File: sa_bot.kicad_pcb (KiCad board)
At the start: 2 copper layers, 120 x 120 mm, 68 parts, among them CON1 MicroSD_Card, P1 USB_OTG, P11 MOTOR_A, P12 MOTOR_B, P13 SONAR_4, P14 SONAR_2, P15 SONAR_3, P17 DBG_CONN, P18 CONN_01X04, P2 BatteryHolder, P3 IR4_JMP, P4 IR2_JMP, P5 IR3_JMP, P6 ExPower, P7 IR_4, P8 IR_2, P9 IR_3, Q1 Q_PMOS_DSG, SW1 SWITCH_INV, SW2 SW_PUSH, SW3 SW_PUSH, SW4 SW_PUSH, U1 74AHC1G125, U2 SAMD21G18, U3 AP2112K-3.3V, U4 NCP1402, U5 DRV8835, Y1 Crystal_Small

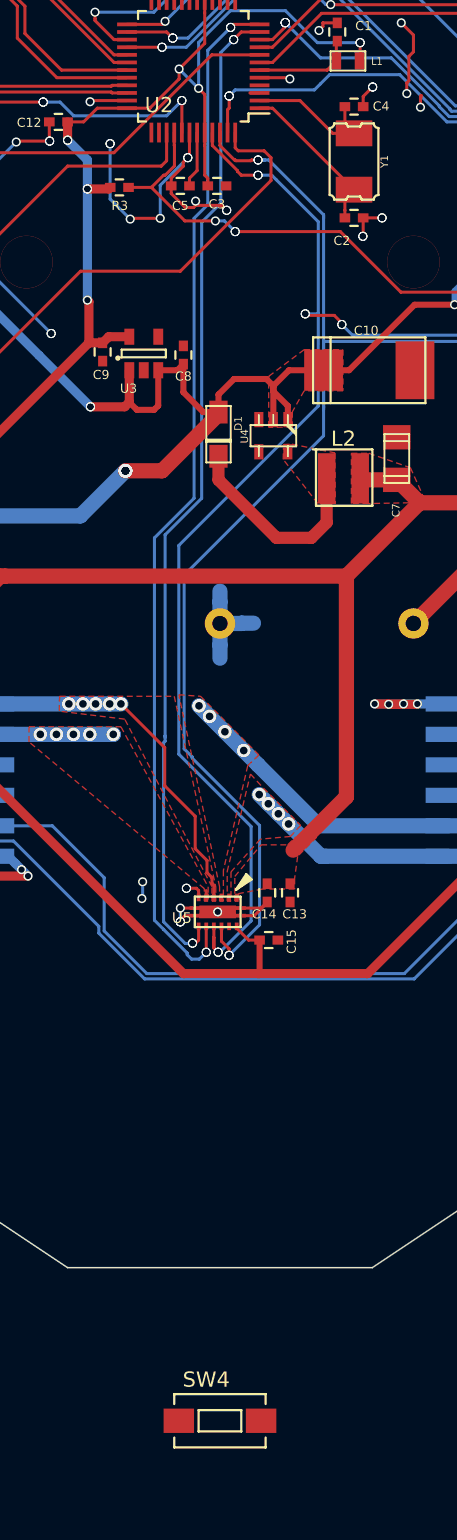
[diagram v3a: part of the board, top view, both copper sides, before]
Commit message: Moved Motor from SWCLK to A0
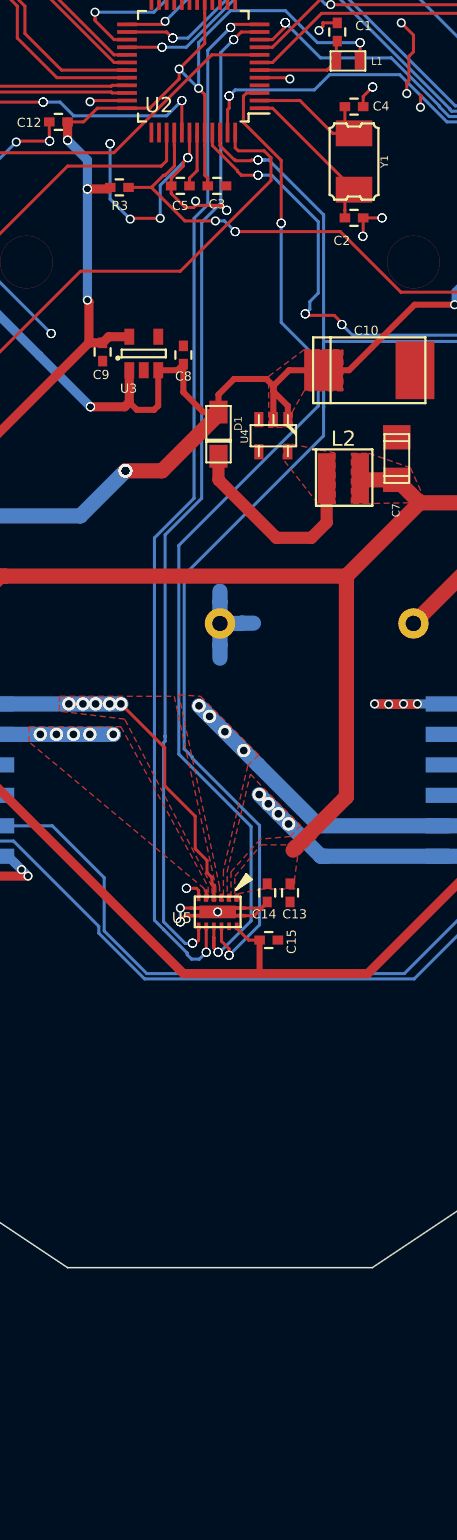
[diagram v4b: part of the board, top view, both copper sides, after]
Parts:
- removed the SW4 at (140.0, 230.1)
- renumbered RESET to SW4
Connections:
- U2 pad 3: Net-(U2-Pad3) -> /AIN2
- U5 pad 9: SWCLK -> /AIN2
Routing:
- net /AIN2: track 0.00 -> 69.1 mm, vias 0 -> 4
- net SWCLK: track 86.1 -> 34.6 mm, vias 8 -> 6
- net (no net): track 7.58 -> 6.42 mm, vias 5 -> 3
- net Net-(U2-Pad3): track 0.64 -> 0.00 mm

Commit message: V002 and firmware
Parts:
- P17: footprint Pin_Headers:Pin_Header_Straight_2x05_Pitch1.27mm -> idlehands_footprints:Pin_Header_Straight_2x05_Pitch1.27mm
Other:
- board text added: "Neural Adaptation Bot v0.02 McMaster University Idle Hands Dev. 11/01/2016"
- board text removed: "Neural Adaptation Bot McMaster University Idle Hands Dev. 04/06/2016"
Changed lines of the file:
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@@
-(kicad_pcb (version 4) (host pcbnew "(2015-07-04 BZR 5884, Git c1bbf3e)-product")
+(kicad_pcb (version 4) (host pcbnew 4.0.4-stable)
   (general
     (links 168)
-    (no_connects 8)
-    (area 79.949999 99.949999 200.050001 220.050001)
+    (no_connects 7)
+    (area 63.774999 83.774999 219.485112 246.000001)
     (thickness 1.6)
     (drawings 17)
@@
     )
   )
-  (module Pin_Headers:Pin_Header_Straight_2x05_Pitch1.27mm (layer F.Cu)
-    (at 164.07 159.2 180)
-    (descr "Through hole pin header, pitch 1.27mm")
-    (tags "pin header")
-    (fp_text reference P17 (at 0.55 -1.7 180) (layer F.SilkS)
-      (effects (font (size 1 1) (thickness 0.15)))
-    )
-    (fp_text value DBG_CONN (at 0 6.9 180) (layer F.Fab)
-      (effects (font (size 1 1) (thickness 0.15)))
-    )
-    (fp_line (start 2.1 -0.8) (end 1.3 -0.8) (layer F.SilkS) (width 0.15))
-    (fp_line (start 2.1 5.85) (end 2.1 -0.8) (layer F.SilkS) (width 0.15))
-    (fp_line (start 2.1 5.85) (end -0.85 5.85) (layer F.SilkS) (width 0.15))
-    (fp_line (start -1.1 -1.05) (end -1.1 6.1) (layer F.CrtYd) (width 0.05))
-    (fp_line (start 2.35 -1.05) (end 2.35 6.1) (layer F.CrtYd) (width 0.05))
-    (fp_line (start -1.1 -1.05) (end 2.35 -1.05) (layer F.CrtYd) (width 0.05))
-    (fp_line (start -1.1 6.1) (end 2.35 6.1) (layer F.CrtYd) (width 0.05))
-    (fp_line (start -0.85 5.85) (end -0.85 1.3) (layer F.SilkS) (width 0.15))
-    (fp_line (start 0.5 -0.8) (end -0.85 -0.8) (layer F.SilkS) (width 0.15))
-    (fp_line (start -0.85 -0.8) (end -0.85 0.5) (layer F.SilkS) (width 0.15))
-    (pad 1 thru_hole rect (at 0 0 180) (size 1.05 1.05) (drill 0.65) (layers *.Cu *.Mask F.SilkS)
-      (net 4 +3V3))
-    (pad 3 thru_hole circle (at 0 1.27 180) (size 1.05 1.05) (drill 0.65) (layers *.Cu *.Mask F.SilkS)
-      (net 2 GND))
-    (pad 5 thru_hole circle (at 0 2.54 180) (size 1.05 1.05) (drill 0.65) (layers *.Cu *.Mask F.SilkS)
-      (net 2 GND))
-    (pad 7 thru_hole circle (at 0 3.81 180) (size 1.05 1.05) (drill 0.65) (layers *.Cu *.Mask F.SilkS)
-      (net 38 "Net-(P17-Pad7)"))
-    (pad 9 thru_hole circle (at 0 5.08 180) (size 1.05 1.05) (drill 0.65) (layers *.Cu *.Mask F.SilkS)
-      (net 39 "Net-(P17-Pad9)"))
-    (pad 4 thru_hole circle (at 1.27 1.27 180) (size 1.05 1.05) (drill 0.65) (layers *.Cu *.Mask F.SilkS)
-      (net 40 SWCLK))
-    (pad 6 thru_hole circle (at 1.27 2.54 180) (size 1.05 1.05) (drill 0.65) (layers *.Cu *.Mask F.SilkS)
-      (net 41 "Net-(P17-Pad6)"))
-    (pad 8 thru_hole circle (at 1.27 3.81 180) (size 1.05 1.05) (drill 0.65) (layers *.Cu *.Mask F.SilkS)
-      (net 42 "Net-(P17-Pad8)"))
-    (pad 10 thru_hole circle (at 1.27 5.08 180) (size 1.05 1.05) (drill 0.65) (layers *.Cu *.Mask F.SilkS)
-      (net 43 RESET))
-    (pad 2 thru_hole circle (at 1.27 0 180) (size 1.05 1.05) (drill 0.65) (layers *.Cu *.Mask F.SilkS)
-      (net 44 SWDIO))
-  )
   (module project_footprints:c_1206 (layer F.Cu)
     (at 116.1 130.6 45)
@@
       (net 43 RESET))
   )
+  (module idlehands_footprints:Pin_Header_Straight_2x05_Pitch1.27mm (layer F.Cu)
+    (at 164.07 159.2 180)
+    (descr "Through hole pin header, pitch 1.27mm")
+    (tags "pin header")
+    (fp_text reference P17 (at 0.55 -1.7 180) (layer F.SilkS)
+      (effects (font (size 1 1) (thickness 0.15)))
+    )
+    (fp_text value DBG_CONN (at 0 6.9 180) (layer F.Fab)
+      (effects (font (size 1 1) (thickness 0.15)))
+    )
+    (fp_line (start -1.4 1.7) (end -0.9 1.7) (layer F.SilkS) (width 0.15))
+    (fp_line (start -1.4 3.4) (end -1.4 1.7) (layer F.SilkS) (width 0.15))
+    (fp_line (start -0.9 3.4) (end -1.4 3.4) (layer F.SilkS) (width 0.15))
+    (fp_line (start 2.1 -0.8) (end 1.3 -0.8) (layer F.SilkS) (width 0.15))
+    (fp_line (start 2.1 5.85) (end 2.1 -0.8) (layer F.SilkS) (width 0.15))
+    (fp_line (start 2.1 5.85) (end -0.85 5.85) (layer F.SilkS) (width 0.15))
+    (fp_line (start -1.1 -1.05) (end -1.1 6.1) (layer F.CrtYd) (width 0.05))
+    (fp_line (start 2.35 -1.05) (end 2.35 6.1) (layer F.CrtYd) (width 0.05))
+    (fp_line (start -1.1 -1.05) (end 2.35 -1.05) (layer F.CrtYd) (width 0.05))
+    (fp_line (start -1.1 6.1) (end 2.35 6.1) (layer F.CrtYd) (width 0.05))
+    (fp_line (start -0.9 5.85) (end -0.9 3.4) (layer F.SilkS) (width 0.15))
+    (fp_line (start 0.5 -0.8) (end -0.85 -0.8) (layer F.SilkS) (width 0.15))
+    (fp_line (start -0.9 -0.8) (end -0.9 1.7) (layer F.SilkS) (width 0.15))
+    (pad 1 thru_hole rect (at 0 0 180) (size 1.05 1.05) (drill 0.65) (layers *.Cu *.Mask F.SilkS)
+      (net 4 +3V3))
+    (pad 3 thru_hole circle (at 0 1.27 180) (size 1.05 1.05) (drill 0.65) (layers *.Cu *.Mask F.SilkS)
+      (net 2 GND))
+    (pad 5 thru_hole circle (at 0 2.54 180) (size 1.05 1.05) (drill 0.65) (layers *.Cu *.Mask F.SilkS)
+      (net 2 GND))
+    (pad 7 thru_hole circle (at 0 3.81 180) (size 1.05 1.05) (drill 0.65) (layers *.Cu *.Mask F.SilkS)
+      (net 38 "Net-(P17-Pad7)"))
+    (pad 9 thru_hole circle (at 0 5.08 180) (size 1.05 1.05) (drill 0.65) (layers *.Cu *.Mask F.SilkS)
+      (net 39 "Net-(P17-Pad9)"))
+    (pad 4 thru_hole circle (at 1.27 1.27 180) (size 1.05 1.05) (drill 0.65) (layers *.Cu *.Mask F.SilkS)
+      (net 40 SWCLK))
+    (pad 6 thru_hole circle (at 1.27 2.54 180) (size 1.05 1.05) (drill 0.65) (layers *.Cu *.Mask F.SilkS)
+      (net 41 "Net-(P17-Pad6)"))
+    (pad 8 thru_hole circle (at 1.27 3.81 180) (size 1.05 1.05) (drill 0.65) (layers *.Cu *.Mask F.SilkS)
+      (net 42 "Net-(P17-Pad8)"))
+    (pad 10 thru_hole circle (at 1.27 5.08 180) (size 1.05 1.05) (drill 0.65) (layers *.Cu *.Mask F.SilkS)
+      (net 43 RESET))
+    (pad 2 thru_hole circle (at 1.27 0 180) (size 1.05 1.05) (drill 0.65) (layers *.Cu *.Mask F.SilkS)
+      (net 44 SWDIO))
+  )
   (gr_text "5V\nGND\nVBATT\n\n" (at 110.8 174.8) (layer B.SilkS)
     (effects (font (size 1.5 1.5) (thickness 0.3)) (justify mirror))
@@
     (effects (font (size 1.5 1.5) (thickness 0.3)))
   )
-  (gr_text "Neural Adaptation Bot\nMcMaster University\nIdle Hands Dev.\n04/06/2016" (at 140.2 214.2) (layer B.SilkS)
+  (gr_text "Neural Adaptation Bot v0.02\nMcMaster University\nIdle Hands Dev.\n11/01/2016" (at 140.2 214.2) (layer B.SilkS)
     (effects (font (size 1.5 1.5) (thickness 0.3)) (justify mirror))
   )
